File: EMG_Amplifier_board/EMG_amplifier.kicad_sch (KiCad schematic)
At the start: 8 parts, among them J1 Conn_01x04_Socket, J2 Conn_01x04_Pin, J3 Conn_01x06_Pin, J4 Conn_01x06_Socket, J7 Conn_01x06_Pin

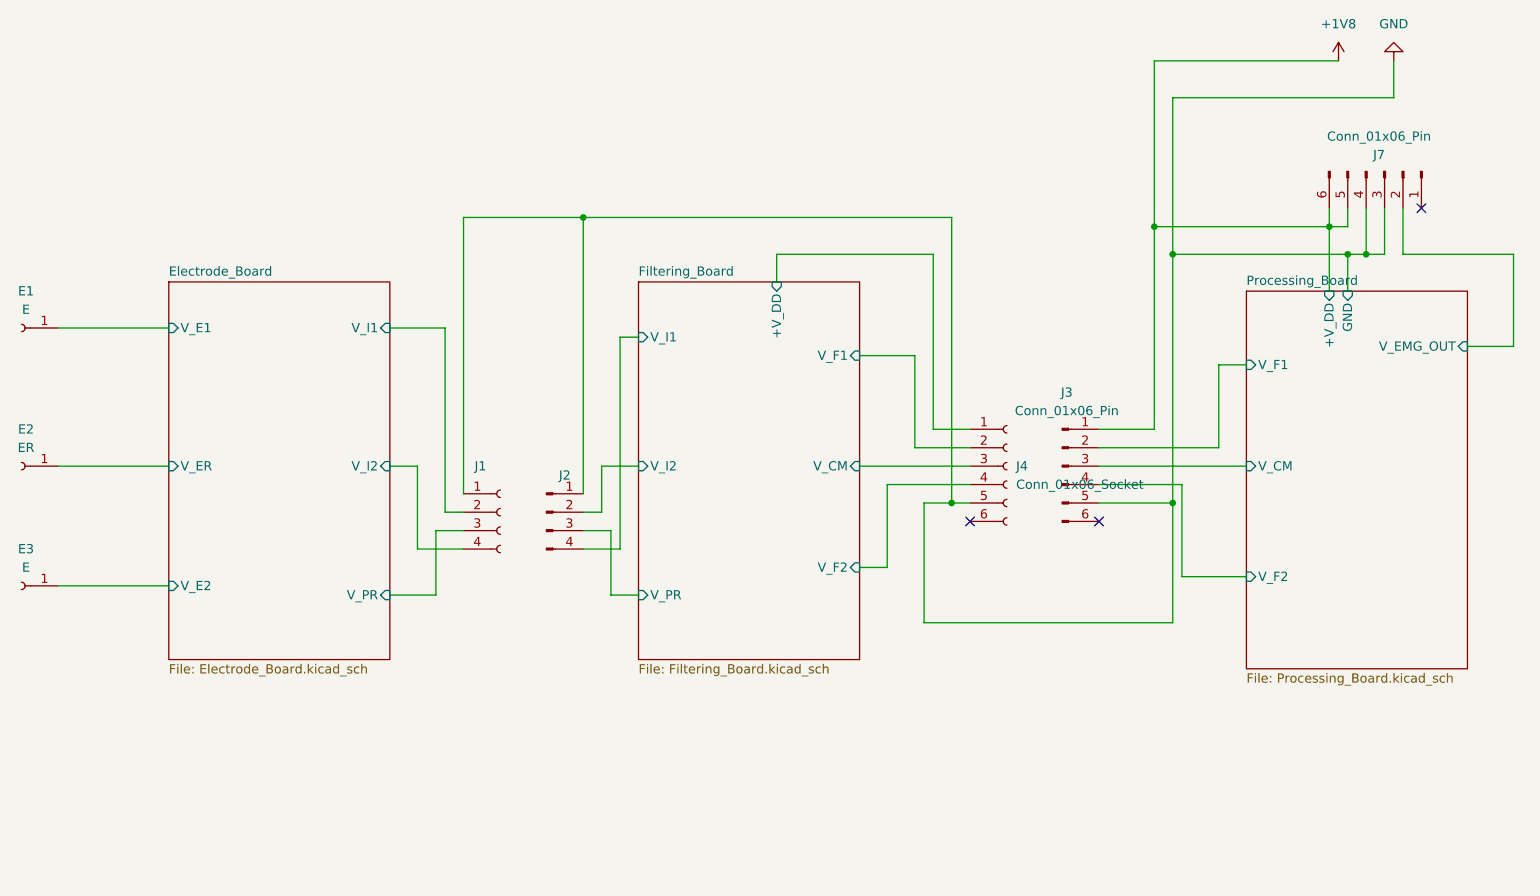
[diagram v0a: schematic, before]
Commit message: add license
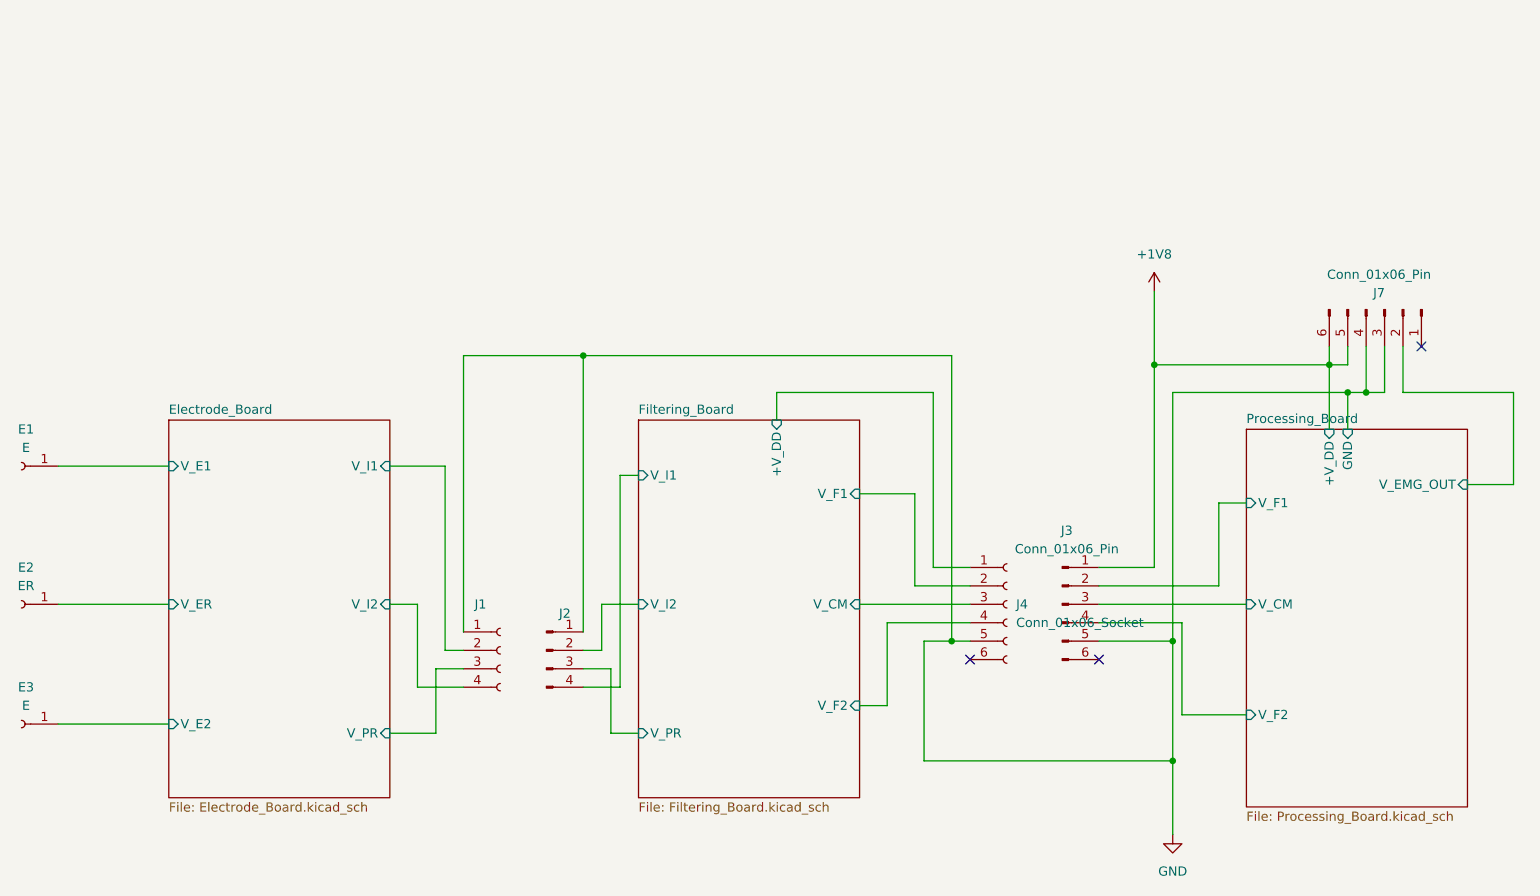
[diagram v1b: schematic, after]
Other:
- moved on the sheet: E1, E2, E3, J1, J2, J3, J4, J7
